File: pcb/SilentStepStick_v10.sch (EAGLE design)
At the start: 30 parts, among them X1 PASSER-07, X2 PASSER-07

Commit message: updated layout and schematics
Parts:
- CFG1, CFG2, CFG3, CFG6: value JUMPER2-0201-NC -> JUMPER2-0201; device we-rcl:JUMPER2-0201-NC -> we-rcl:JUMPER2-0201
- CFG5: value JUMPER3-0201-NC -> JUMPER3-0201; device we-rcl:JUMPER3-0201-NC -> we-rcl:JUMPER3-0201
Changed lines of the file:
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@@
 <setting verticaltext="up"/>
 </settings>
-<grid distance="0.05" unitdist="inch" unit="inch" style="lines" multiple="1" display="yes" altdistance="0.025" altunitdist="inch" altunit="inch"/>
+<grid distance="0.1" unitdist="inch" unit="inch" style="lines" multiple="1" display="no" altdistance="0.01" altunitdist="inch" altunit="inch"/>
 <layers>
-<layer number="1" name="Top" color="4" fill="1" visible="no" active="no"/>
-<layer number="2" name="Route2" color="11" fill="1" visible="no" active="no"/>
-<layer number="3" name="Route3" color="4" fill="3" visible="no" active="no"/>
-<layer number="4" name="Route4" color="1" fill="4" visible="no" active="no"/>
-<layer number="5" name="Route5" color="4" fill="4" visible="no" active="no"/>
-<layer number="6" name="Route6" color="1" fill="8" visible="no" active="no"/>
-<layer number="7" name="Route7" color="4" fill="8" visible="no" active="no"/>
-<layer number="8" name="Route8" color="1" fill="2" visible="no" active="no"/>
-<layer number="9" name="Route9" color="4" fill="2" visible="no" active="no"/>
-<layer number="10" name="Route10" color="1" fill="7" visible="no" active="no"/>
-<layer number="11" name="Route11" color="4" fill="7" visible="no" active="no"/>
-<layer number="12" name="Route12" color="1" fill="5" visible="no" active="no"/>
-<layer number="13" name="Route13" color="4" fill="5" visible="no" active="no"/>
-<layer number="14" name="Route14" color="1" fill="6" visible="no" active="no"/>
-<layer number="15" name="Route15" color="13" fill="1" visible="no" active="no"/>
-<layer number="16" name="Bottom" color="1" fill="1" visible="no" active="no"/>
-<layer number="17" name="Pads" color="2" fill="1" visible="no" active="no"/>
-<layer number="18" name="Vias" color="2" fill="1" visible="no" active="no"/>
-<layer number="19" name="Unrouted" color="14" fill="1" visible="no" active="no"/>
-<layer number="20" name="Dimension" color="15" fill="1" visible="no" active="no"/>
-<layer number="21" name="tPlace" color="7" fill="1" visible="no" active="no"/>
-<layer number="22" name="bPlace" color="7" fill="1" visible="no" active="no"/>
-<layer number="23" name="tOrigins" color="15" fill="1" visible="no" active="no"/>
-<layer number="24" name="bOrigins" color="15" fill="1" visible="no" active="no"/>
-<layer number="25" name="tNames" color="7" fill="1" visible="no" active="no"/>
-<layer number="26" name="bNames" color="7" fill="1" visible="no" active="no"/>
-<layer number="27" name="tValues" color="7" fill="1" visible="no" active="no"/>
-<layer number="28" name="bValues" color="7" fill="1" visible="no" active="no"/>
+<layer number="1" name="Top" color="4" fill="1" visible="yes" active="no"/>
+<layer number="2" name="Route2" color="11" fill="1" visible="yes" active="no"/>
+<layer number="3" name="Route3" color="4" fill="3" visible="yes" active="no"/>
+<layer number="4" name="Route4" color="1" fill="4" visible="yes" active="no"/>
+<layer number="5" name="Route5" color="4" fill="4" visible="yes" active="no"/>
+<layer number="6" name="Route6" color="1" fill="8" visible="yes" active="no"/>
+<layer number="7" name="Route7" color="4" fill="8" visible="yes" active="no"/>
+<layer number="8" name="Route8" color="1" fill="2" visible="yes" active="no"/>
+<layer number="9" name="Route9" color="4" fill="2" visible="yes" active="no"/>
+<layer number="10" name="Route10" color="1" fill="7" visible="yes" active="no"/>
+<layer number="11" name="Route11" color="4" fill="7" visible="yes" active="no"/>
+<layer number="12" name="Route12" color="1" fill="5" visible="yes" active="no"/>
+<layer number="13" name="Route13" color="4" fill="5" visible="yes" active="no"/>
+<layer number="14" name="Route14" color="1" fill="6" visible="yes" active="no"/>
+<layer number="15" name="Route15" color="13" fill="1" visible="yes" active="no"/>
+<layer number="16" name="Bottom" color="1" fill="1" visible="yes" active="no"/>
+<layer number="17" name="Pads" color="2" fill="1" visible="yes" active="no"/>
+<layer number="18" name="Vias" color="2" fill="1" visible="yes" active="no"/>
+<layer number="19" name="Unrouted" color="14" fill="1" visible="yes" active="no"/>
+<layer number="20" name="Dimension" color="15" fill="1" visible="yes" active="no"/>
+<layer number="21" name="tPlace" color="7" fill="1" visible="yes" active="no"/>
+<layer number="22" name="bPlace" color="7" fill="1" visible="yes" active="no"/>
+<layer number="23" name="tOrigins" color="15" fill="1" visible="yes" active="no"/>
+<layer number="24" name="bOrigins" color="15" fill="1" visible="yes" active="no"/>
+<layer number="25" name="tNames" color="7" fill="1" visible="yes" active="no"/>
+<layer number="26" name="bNames" color="7" fill="1" visible="yes" active="no"/>
+<layer number="27" name="tValues" color="7" fill="1" visible="yes" active="no"/>
+<layer number="28" name="bValues" color="7" fill="1" visible="yes" active="no"/>
 <layer number="29" name="tStop" color="7" fill="3" visible="no" active="no"/>
 <layer number="30" name="bStop" color="7" fill="6" visible="no" active="no"/>
@@
 <layer number="35" name="tGlue" color="7" fill="4" visible="no" active="no"/>
 <layer number="36" name="bGlue" color="7" fill="5" visible="no" active="no"/>
-<layer number="37" name="tTest" color="7" fill="1" visible="no" active="no"/>
-<layer number="38" name="bTest" color="7" fill="1" visible="no" active="no"/>
+<layer number="37" name="tTest" color="7" fill="1" visible="yes" active="no"/>
+<layer number="38" name="bTest" color="7" fill="1" visible="yes" active="no"/>
 <layer number="39" name="tKeepout" color="4" fill="11" visible="no" active="no"/>
 <layer number="40" name="bKeepout" color="1" fill="11" visible="no" active="no"/>
@@
 <layer number="44" name="Drills" color="7" fill="1" visible="no" active="no"/>
 <layer number="45" name="Holes" color="7" fill="1" visible="no" active="no"/>
-<layer number="46" name="Milling" color="3" fill="1" visible="no" active="no"/>
-<layer number="47" name="Measures" color="7" fill="1" visible="no" active="no"/>
-<layer number="48" name="Document" color="7" fill="1" visible="no" active="no"/>
-<layer number="49" name="Reference" color="7" fill="1" visible="no" active="no"/>
-<layer number="50" name="dxf" color="7" fill="1" visible="no" active="no"/>
-<layer number="51" name="tDocu" color="7" fill="1" visible="no" active="no"/>
-<layer number="52" name="bDocu" color="7" fill="1" visible="no" active="no"/>
-<layer number="53" name="tPadExt" color="7" fill="6" visible="no" active="no"/>
-<layer number="54" name="bPadExt" color="1" fill="3" visible="no" active="no"/>
-<layer number="56" name="wert" color="7" fill="1" visible="no" active="no"/>
-<layer number="57" name="tCAD" color="7" fill="1" visible="no" active="no"/>
+<layer number="46" name="Milling" color="3" fill="1" visible="yes" active="no"/>
+<layer number="47" name="Measures" color="7" fill="1" visible="yes" active="no"/>
+<layer number="48" name="Document" color="7" fill="1" visible="yes" active="no"/>
+<layer number="49" name="Reference" color="7" fill="1" visible="yes" active="no"/>
+<layer number="50" name="dxf" color="7" fill="1" visible="yes" active="no"/>
+<layer number="51" name="tDocu" color="7" fill="1" visible="yes" active="no"/>
+<layer number="52" name="bDocu" color="7" fill="1" visible="yes" active="no"/>
+<layer number="53" name="tPadExt" color="7" fill="6" visible="yes" active="no"/>
+<layer number="54" name="bPadExt" color="1" fill="3" visible="yes" active="no"/>
+<layer number="56" name="wert" color="7" fill="1" visible="yes" active="no"/>
+<layer number="57" name="tCAD" color="7" fill="1" visible="yes" active="no"/>
 <layer number="91" name="Nets" color="2" fill="1" visible="yes" active="yes"/>
 <layer number="92" name="Busses" color="1" fill="1" visible="yes" active="yes"/>
@@
 <part name="GND15" library="supply1" deviceset="GND" device=""/>
 <part name="P+3" library="supply1" deviceset="+5V" device=""/>
-<part name="CFG3" library="we-rcl" deviceset="JUMPER2" device="-0201-NC"/>
+<part name="CFG3" library="we-rcl" deviceset="JUMPER2" device="-0201" value="JUMPER2-0201"/>
 <part name="CFG4" library="we-rcl" deviceset="JUMPER3" device="-0201-NC"/>
-<part name="CFG5" library="we-rcl" deviceset="JUMPER3" device="-0201-NC"/>
-<part name="CFG6" library="we-rcl" deviceset="JUMPER2" device="-0201-NC"/>
-<part name="CFG1" library="we-rcl" deviceset="JUMPER2" device="-0201-NC"/>
-<part name="CFG2" library="we-rcl" deviceset="JUMPER2" device="-0201-NC"/>
+<part name="CFG5" library="we-rcl" deviceset="JUMPER3" device="-0201" value="JUMPER3-0201"/>
+<part name="CFG6" library="we-rcl" deviceset="JUMPER2" device="-0201" value="JUMPER2-0201"/>
+<part name="CFG1" library="we-rcl" deviceset="JUMPER2" device="-0201" value="JUMPER2-0201"/>
+<part name="CFG2" library="we-rcl" deviceset="JUMPER2" device="-0201" value="JUMPER2-0201"/>
 <part name="R3" library="rcl" deviceset="R-EU_" device="R0402" value="R0402/0"/>
 <part name="R6" library="we-rcl" deviceset="POT" device="EVM3R"/>
@@
 stealthChop
 stealthChop</text>
+<wire x1="59.055" y1="31.75" x2="60.325" y2="31.75" width="1.016" layer="94"/>
+<wire x1="59.055" y1="24.13" x2="60.325" y2="24.13" width="1.016" layer="94"/>
 </plain>
 <instances>

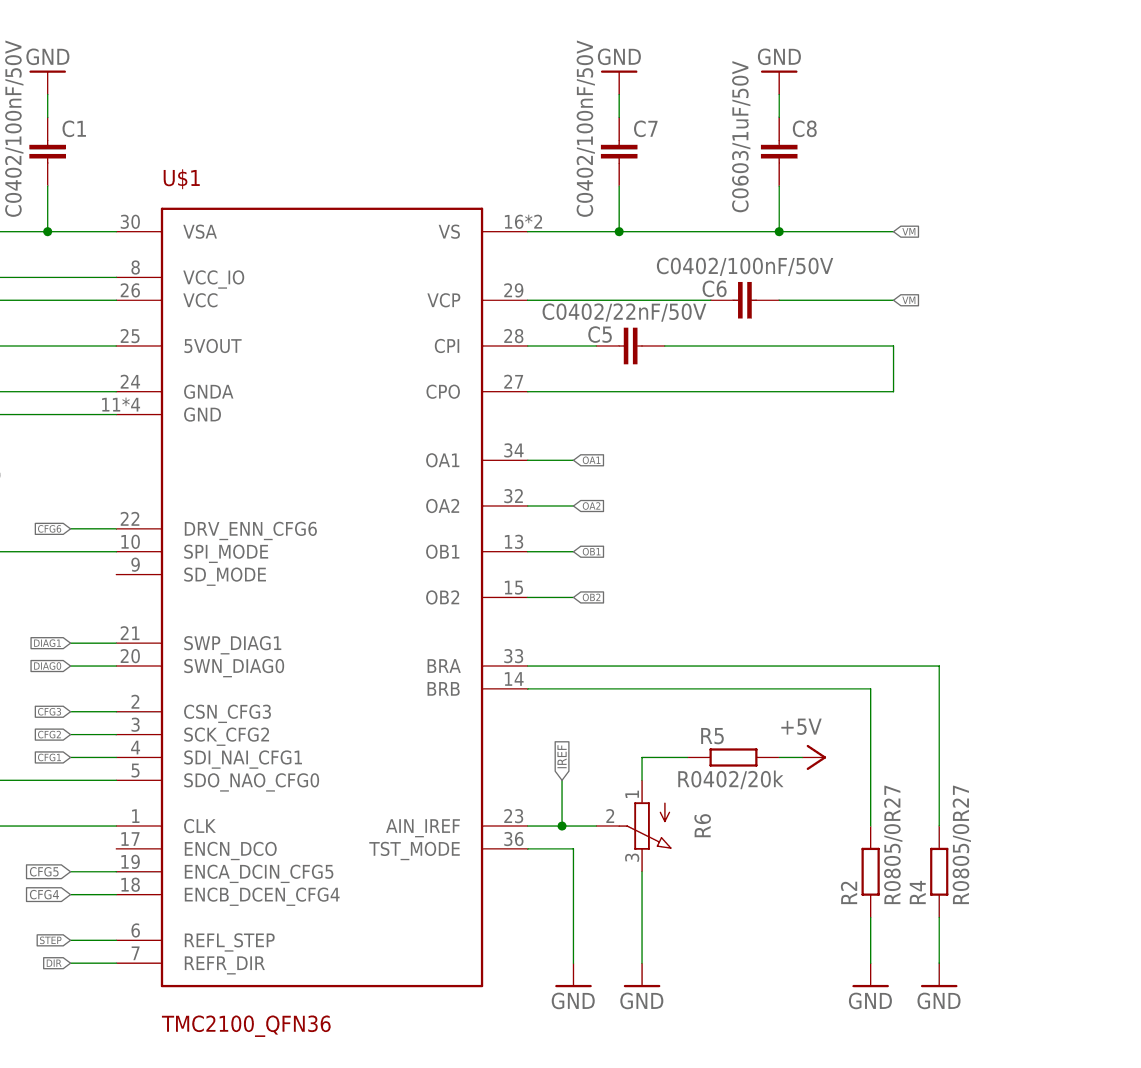
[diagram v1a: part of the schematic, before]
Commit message: updated schematics
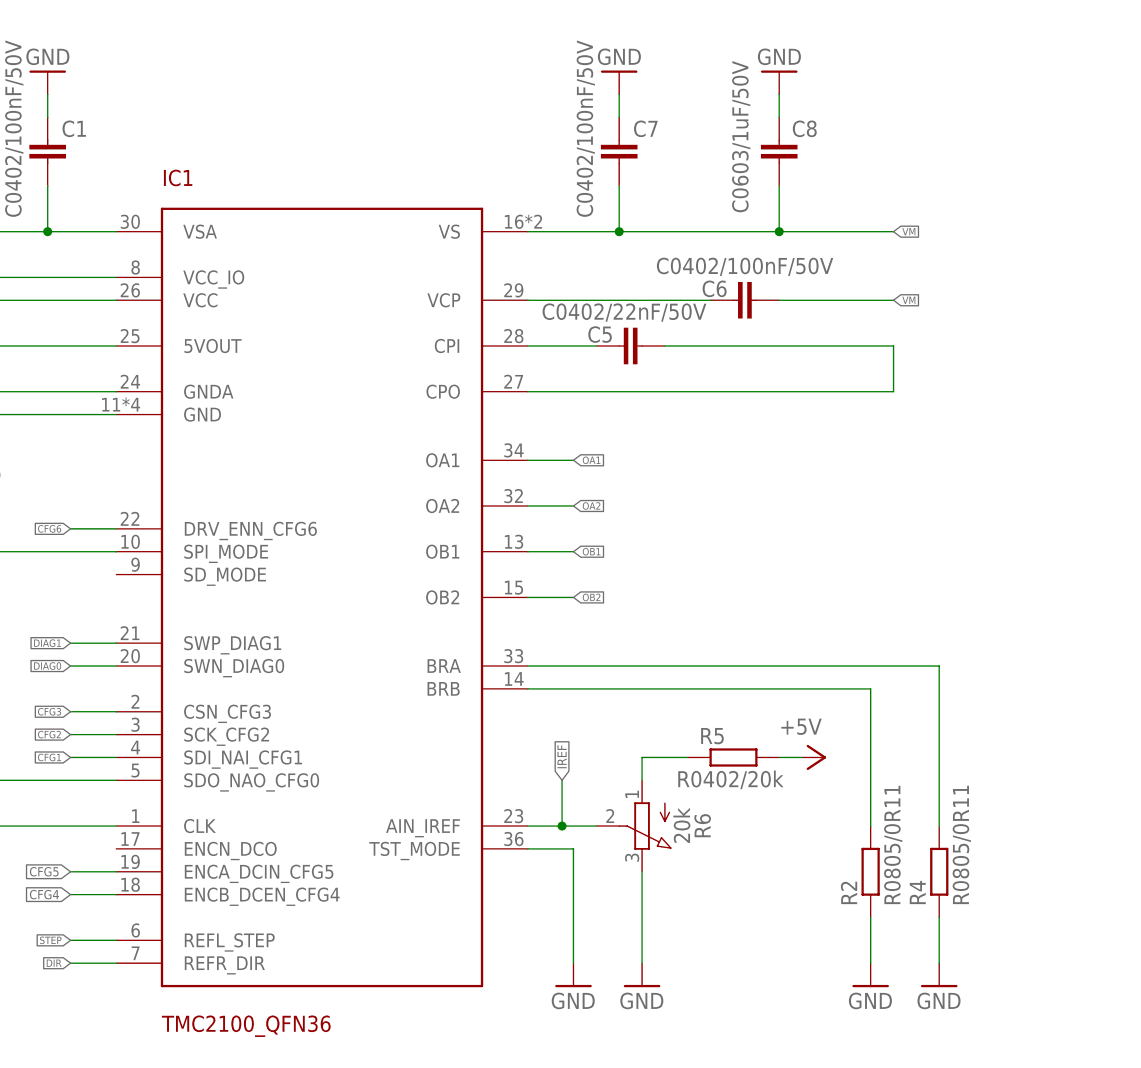
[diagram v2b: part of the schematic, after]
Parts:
- R2, R4: value R0805/0R27 -> R0805/0R11
- R6: value (none) -> 20k
- renumbered U$1 to IC1
